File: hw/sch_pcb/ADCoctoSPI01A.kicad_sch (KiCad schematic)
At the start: 79 parts, among them J1 +5V, J10 HEADER_1x02, J11 HEADER_2x04, J2 SATA7-67491-1030, J3 SATA7-67491-1030, J4 SATA7-67491-1030, J5 SATA7-67491-1030, J6 SAS_mini_1888174, J7 SATA7-67491-1030, J8 HEADER_1x02, J9 HEADER_1x02, M1 HOLE, M2 HOLE, M3 HOLE, M4 HOLE, U1 AFE5801, U2 LM1117MP-1,8/NO, U3 LM1117MP-3,3/NO

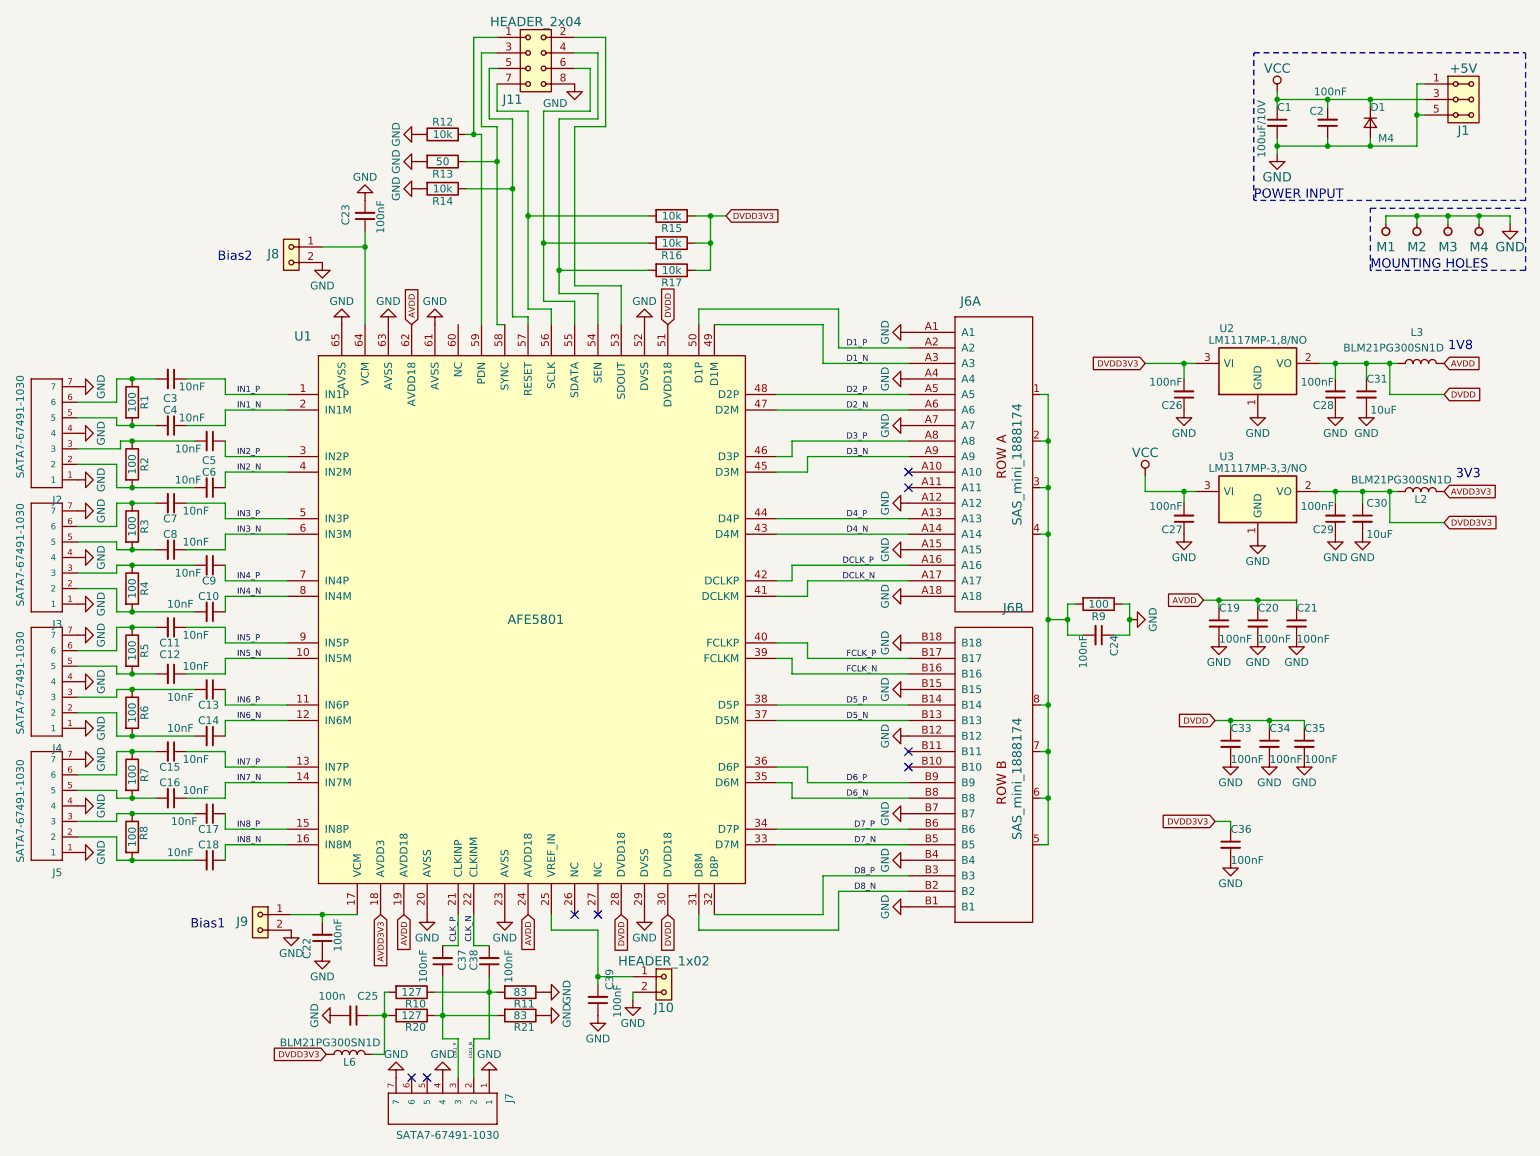
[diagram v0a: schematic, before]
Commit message: Repository cleanup Update of KiCAD project version to 6.0.1.
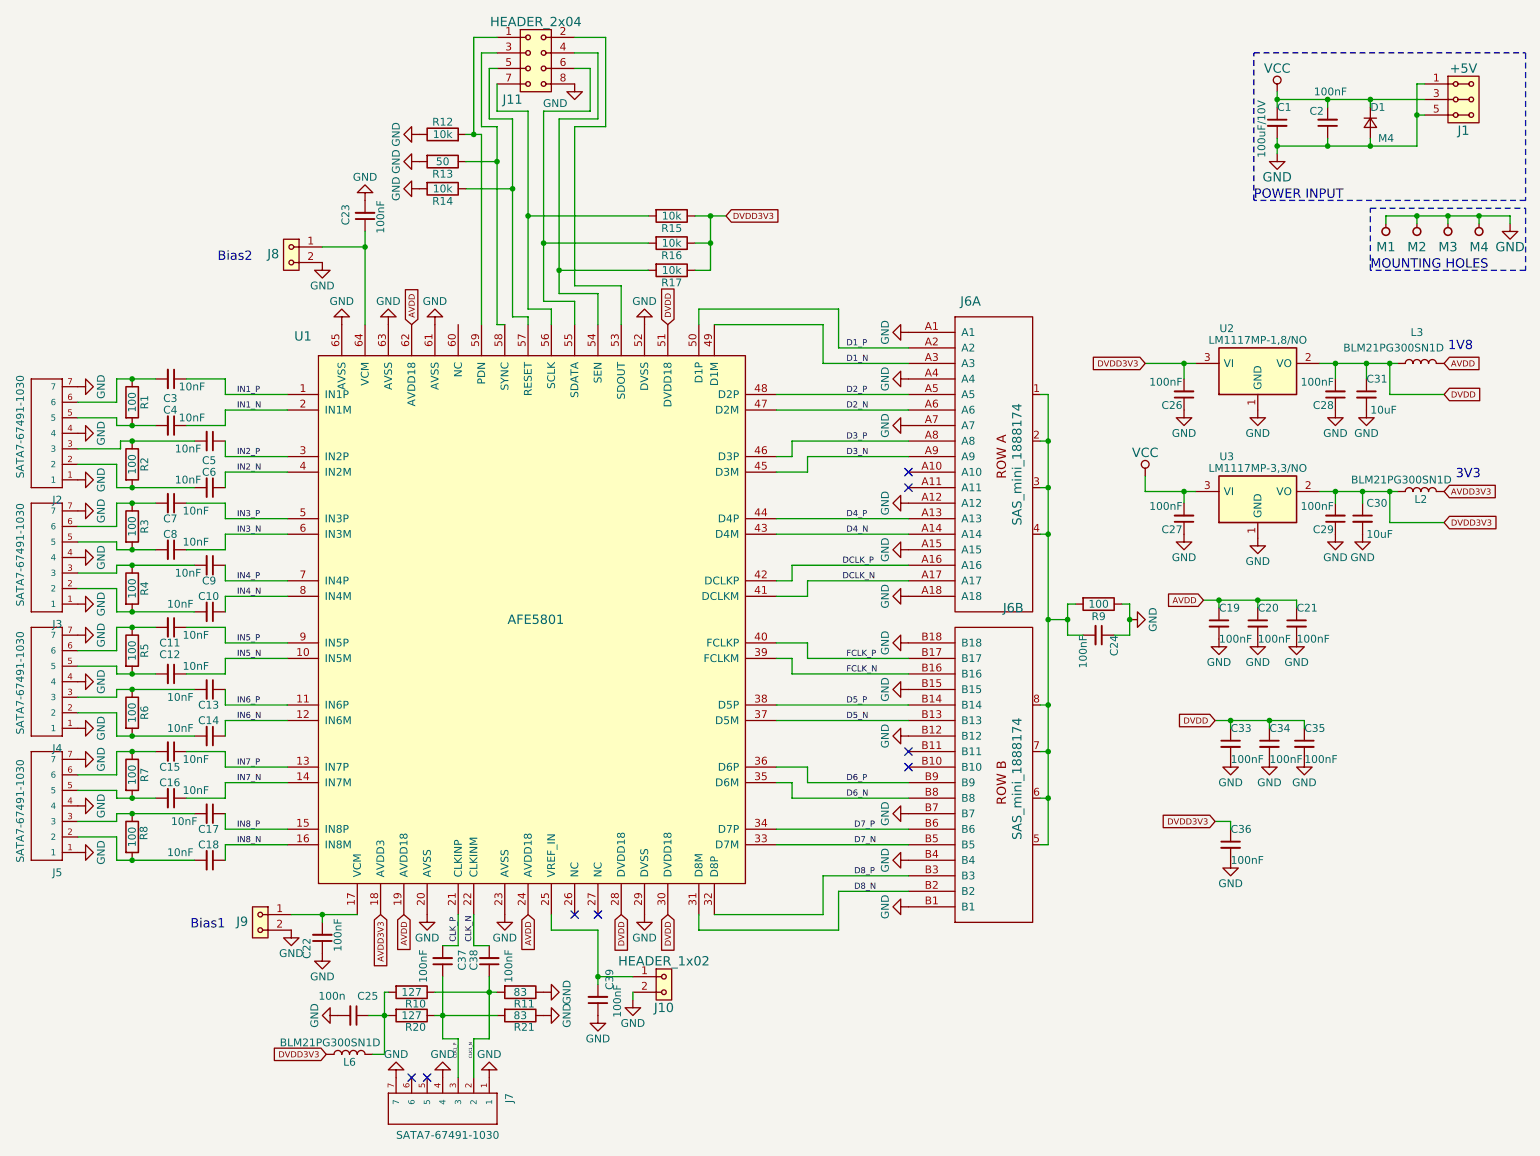
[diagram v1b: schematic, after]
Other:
- company: ORBISYS www.orbisys.sk -> Maksim Rezenov, Jakub kakona

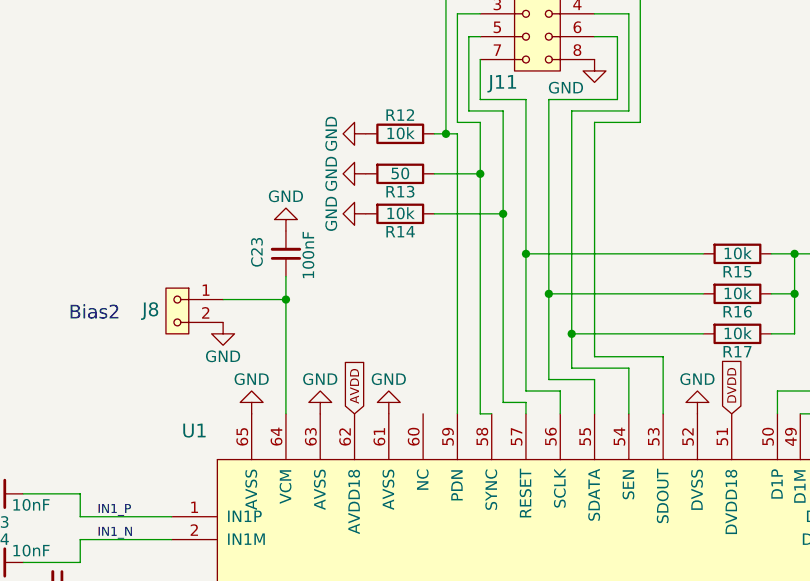
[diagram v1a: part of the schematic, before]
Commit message: Add a link to schematics.
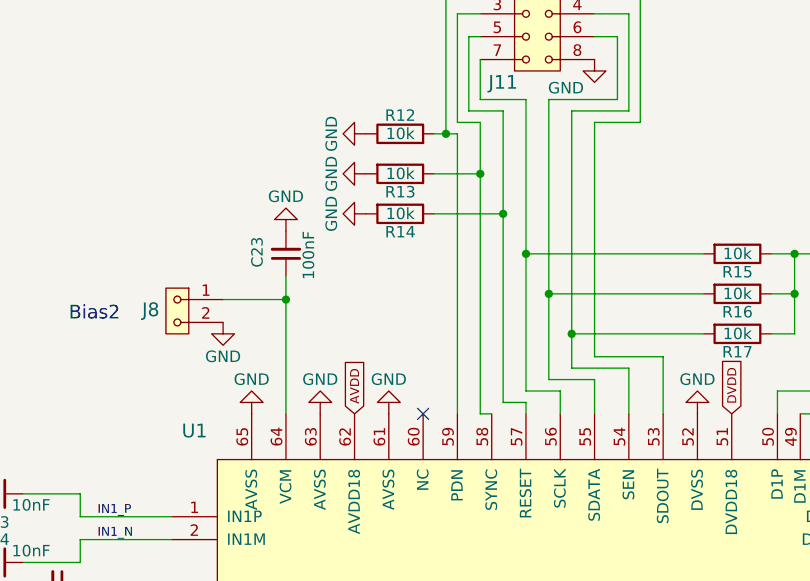
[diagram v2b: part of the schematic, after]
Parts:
- R13: value 50 -> 10k
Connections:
- no-connect marks 8 -> 9
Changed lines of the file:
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@@
   (no_connect (at 95.885 186.69))
   (no_connect (at 177.165 87.63))
+  (no_connect (at 103.505 63.5))
   (no_connect (at 126.365 160.02))
   (no_connect (at 177.165 90.17))
@@
       (effects (font (size 1.524 1.524)) hide)
     )
-    (property "Datasheet" "" (id 3) (at 99.695 62.23 0)
+    (property "Datasheet" "https://www.ti.com/lit/ds/symlink/afe5801.pdf" (id 3) (at 99.695 62.23 0)
       (effects (font (size 1.524 1.524)) hide)
     )
@@
     (in_bom yes) (on_board yes)
     (property "Reference" "R13" (id 0) (at 100.965 38.862 90))
-    (property "Value" "50" (id 1) (at 100.965 36.83 90))
+    (property "Value" "10k" (id 1) (at 100.965 36.83 90))
     (property "Footprint" "Mlab_R:SMD-0603" (id 2) (at 100.965 35.052 90)
       (effects (font (size 1.27 1.27)) hide)
@@
     )
     (path "/00000000-0000-0000-0000-000059d91f98"
-      (reference "R13") (unit 1) (value "50") (footprint "Mlab_R:SMD-0603")
+      (reference "R13") (unit 1) (value "10k") (footprint "Mlab_R:SMD-0603")
     )
     (path "/00000000-0000-0000-0000-000059d91b4a"

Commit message: Update footprints.
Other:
- company: Maksim Rezenov, Jakub kakona -> Mlab.cz
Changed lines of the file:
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@@
   (title_block
     (title "ADCoctoSPI01A")
-    (date "%F")
-    (rev "REV 0.2")
-    (company "Maksim Rezenov, Jakub kakona")
+    (date "2022-03-24")
+    (company "Mlab.cz")
     (comment 2 "Serial LVDS output 8-channel 12bit ADC")
   )
@@
       (effects (font (size 1.524 1.524)))
     )
+    (pin "1")
+    (pin "2")
+    (pin "3")
+    (pin "4")
+    (pin "A1")
+    (pin "A10")
+    (pin "A11")
+    (pin "A12")
+    (pin "A13")
+    (pin "A14")
+    (pin "A15")
+    (pin "A16")
+    (pin "A17")
+    (pin "A18")
+    (pin "A2")
+    (pin "A3")
+    (pin "A4")
+    (pin "A5")
+    (pin "A6")
+    (pin "A7")
+    (pin "A8")
+    (pin "A9")
     (pin "5")
     (pin "6")
@@
     (pin "A8")
     (pin "A9")
+    (pin "5")
+    (pin "6")
+    (pin "7")
+    (pin "8")
+    (pin "B1")
+    (pin "B10")
+    (pin "B11")
+    (pin "B12")
+    (pin "B13")
+    (pin "B14")
+    (pin "B15")
+    (pin "B16")
+    (pin "B17")
+    (pin "B18")
+    (pin "B2")
+    (pin "B3")
+    (pin "B4")
+    (pin "B5")
+    (pin "B6")
+    (pin "B7")
+    (pin "B8")
+    (pin "B9")
   )
   (symbol (lib_id "ADCoctoSPI01A-rescue:GND-power") (at 41.275 73.66 90) (unit 1)

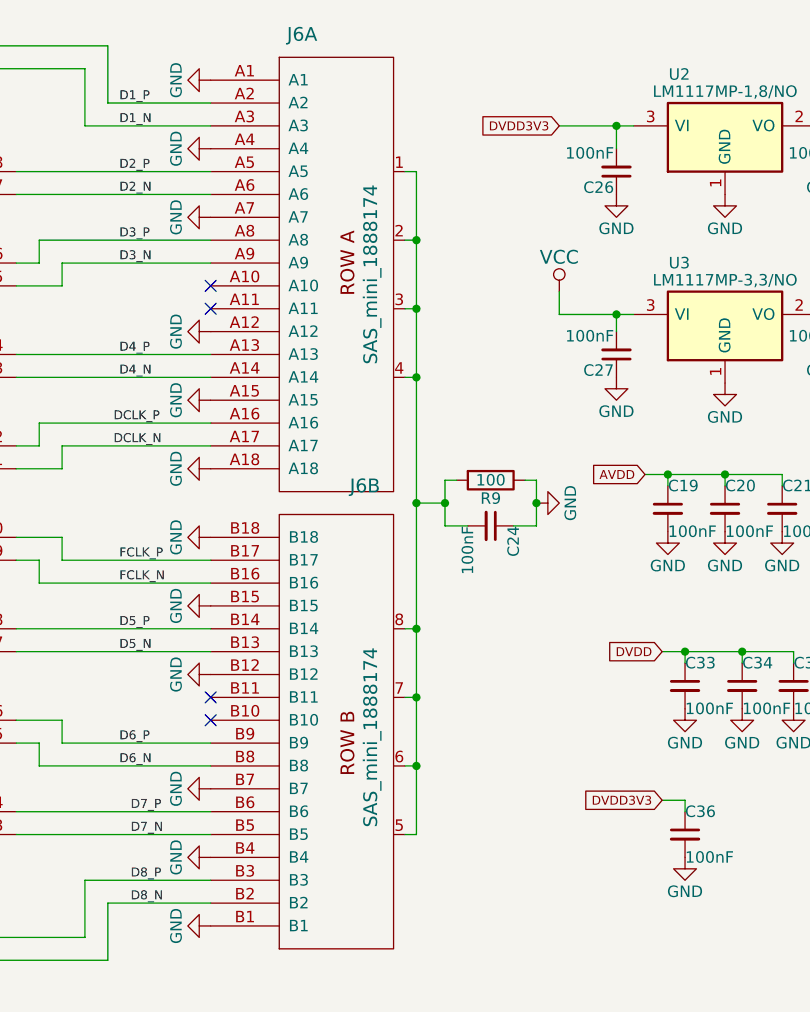
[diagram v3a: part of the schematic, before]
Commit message: Update mini SAS connector footprint to up to date footprint from KiCAD library.
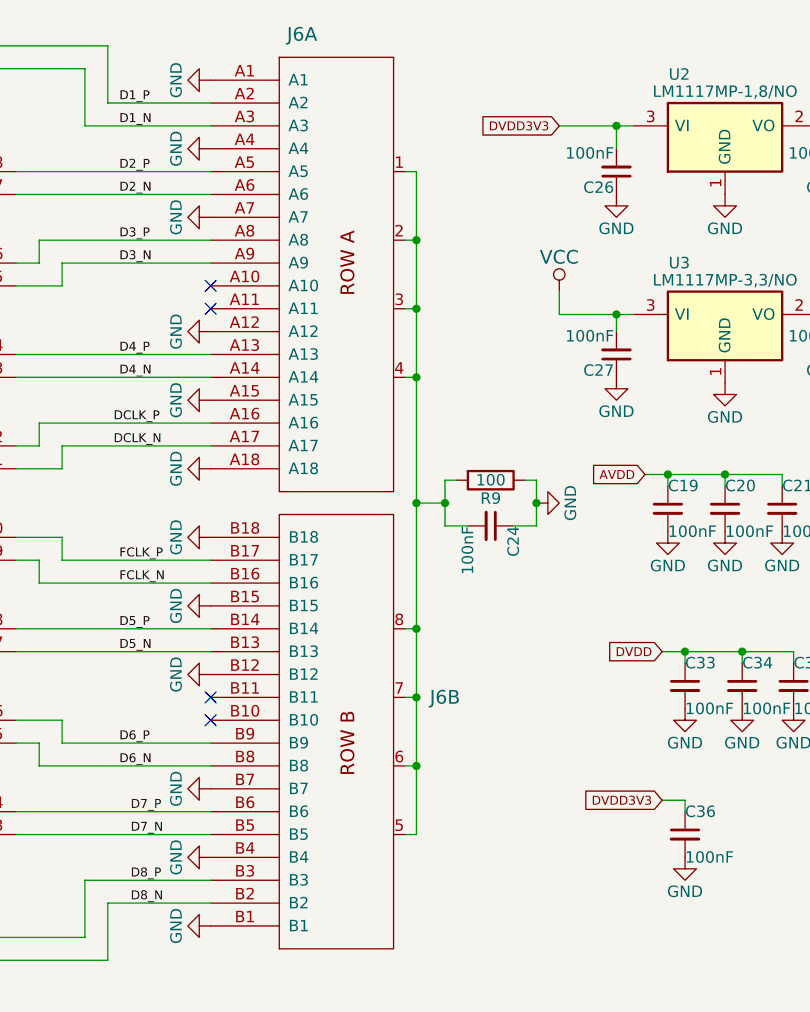
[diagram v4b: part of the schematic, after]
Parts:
- J6: value SAS_mini_1888174 -> (none)
- J6: value SAS_mini_1888174 -> (none); footprint Mlab_CON:SAS_mini_1888174 -> (none)
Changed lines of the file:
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@@
   (symbol (lib_id "ADCoctoSPI01A-rescue:SAS_mini_1888174-MLAB_CONNECTORS") (at 197.485 120.65 0) (mirror x) (unit 2)
     (in_bom yes) (on_board yes)
-    (property "Reference" "J6" (id 0) (at 194.31 109.855 0)
-      (effects (font (size 1.524 1.524)))
-    )
-    (property "Value" "SAS_mini_1888174" (id 1) (at 194.945 137.795 90)
+    (property "Reference" "J6" (id 0) (at 203.2 133.35 0)
+      (effects (font (size 1.524 1.524)))
+    )
+    (property "Value" "" (id 1) (at 194.945 137.795 90)
       (effects (font (size 1.524 1.524)))
     )
     (property "Footprint" "" (id 2) (at 207.645 119.38 0)
-      (effects (font (size 1.524 1.524)))
+      (effects (font (size 1.524 1.524)) hide)
     )
     (property "Datasheet" "" (id 3) (at 207.645 119.38 0)
@@
       (effects (font (size 1.524 1.524)))
     )
-    (property "Value" "SAS_mini_1888174" (id 1) (at 194.945 86.36 90)
-      (effects (font (size 1.524 1.524)))
-    )
-    (property "Footprint" "Mlab_CON:SAS_mini_1888174" (id 2) (at 207.645 104.14 0)
+    (property "Value" "" (id 1) (at 194.945 86.36 90)
+      (effects (font (size 1.524 1.524)))
+    )
+    (property "Footprint" "" (id 2) (at 207.645 104.14 0)
       (effects (font (size 1.524 1.524)) hide)
     )
@@
     )
     (path "/00000000-0000-0000-0000-0000599b64a6"
-      (reference "J6") (unit 1) (value "SAS_mini_1888174") (footprint "Mlab_CON:SAS_mini_1888174")
+      (reference "J6") (unit 1) (value "SAS_mini_1888174") (footprint "Connector_SATA_SAS:SAS-mini_TEConnectivity_1888174_Vertical")
     )
     (path "/00000000-0000-0000-0000-0000599b2682"
-      (reference "J6") (unit 2) (value "SAS_mini_1888174") (footprint "")
+      (reference "J6") (unit 2) (value "SAS_mini_1888174") (footprint "Connector_SATA_SAS:SAS-mini_TEConnectivity_1888174_Vertical")
     )
     (path "/00000000-0000-0000-0000-000059d358b2"
